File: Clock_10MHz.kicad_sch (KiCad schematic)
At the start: 12 parts, among them U3 74LV8154, U4 74LS151, U8 PCF8574, X1 ASCO

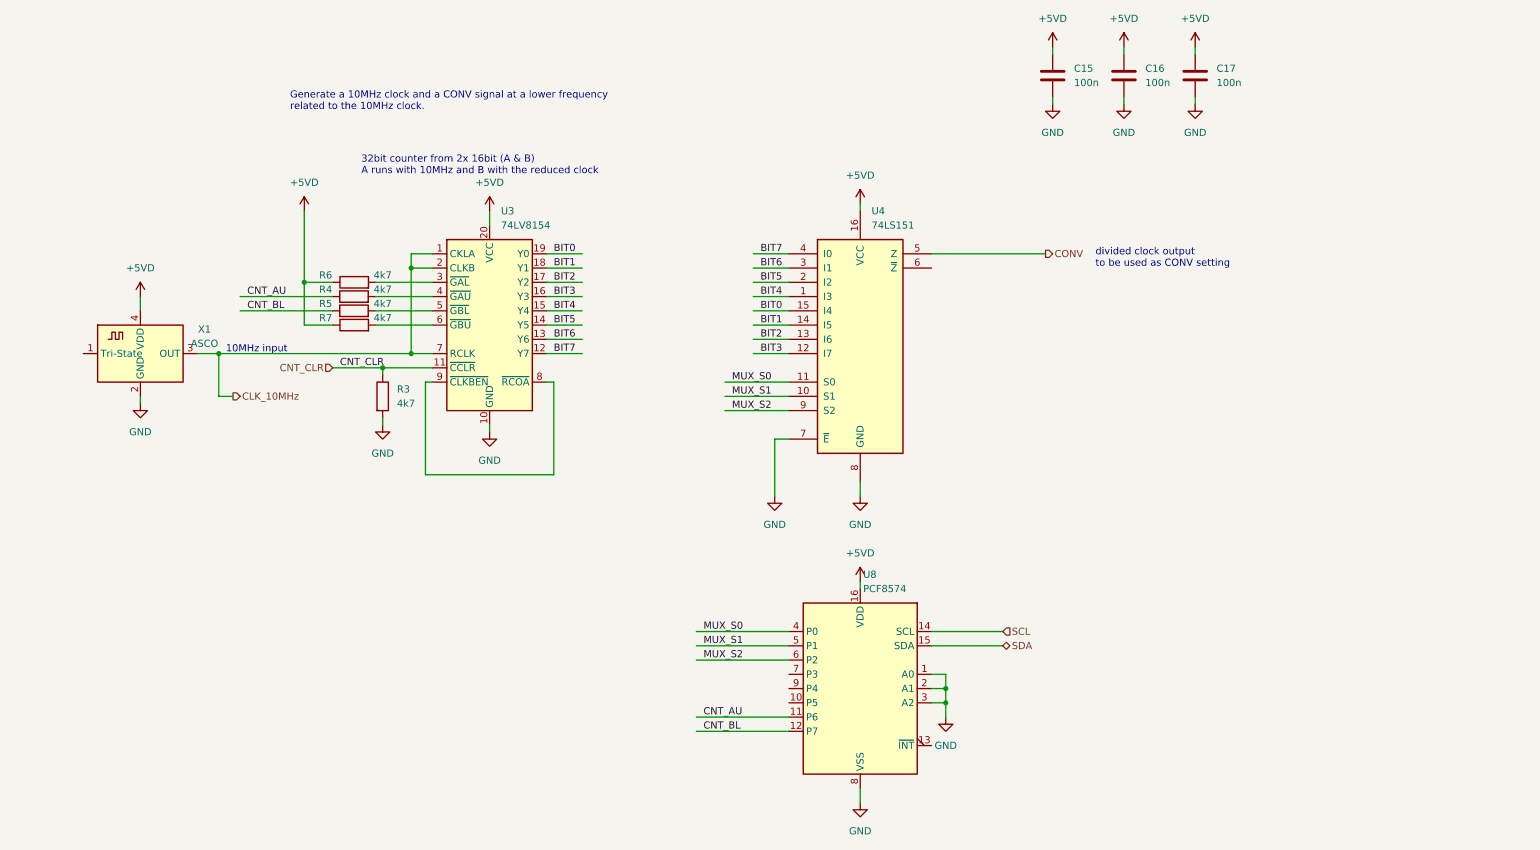
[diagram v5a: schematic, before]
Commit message: updated 10MHz oscillator to DIP 14 package
needs larger PCB space, but much easier to purchase
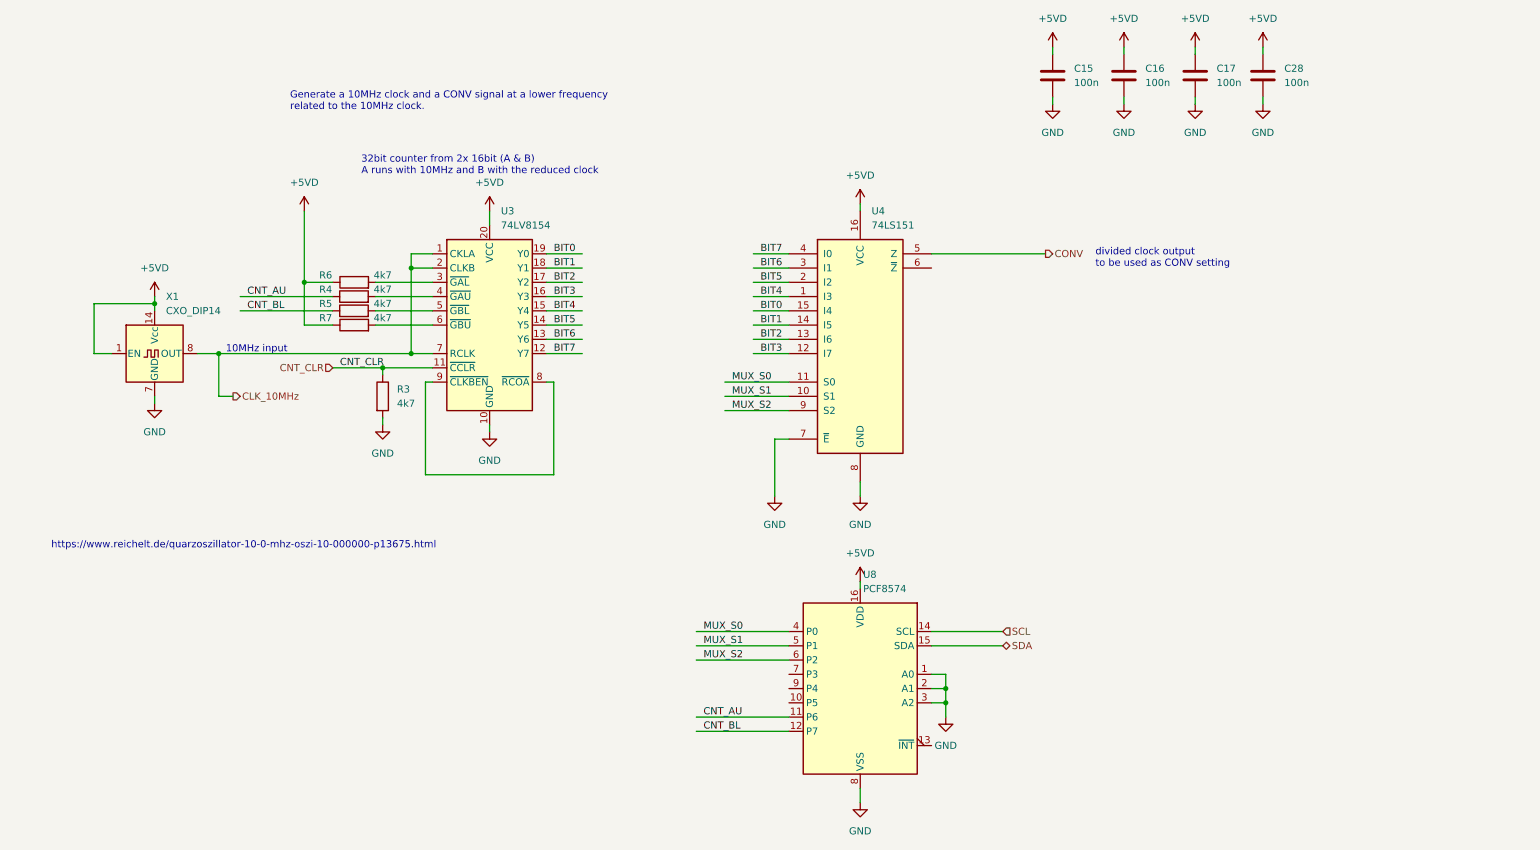
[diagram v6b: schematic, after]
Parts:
- removed X1: ASCO, Oscillator:Oscillator_SMD_Abracon_ASCO-4Pin_1.6x1.2mm, symbol Oscillator:ASCO
- added C28: 100n, Capacitor_SMD:C_0603_1608Metric, symbol Device:C
- added X1: CXO_DIP14, Oscillator:Oscillator_DIP-14, symbol Oscillator:CXO_DIP14
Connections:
- net +5VD: now also C28.1, X1.1 (EN), X1.14 (Vcc)
- net CLK_10MHz: now also X1.8 (OUT)
- net GND: now also C28.2, X1.7 (GND)
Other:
- note added: "https://www.reichelt.de/quarzoszillator-10-0-mhz-oszi-10-000000-p13675.html"
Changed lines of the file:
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@@
   (junction (at 85.09 90.17) (diameter 0) (color 0 0 0 0)
   )
+  (junction (at 39.37 81.28) (diameter 0) (color 0 0 0 0)
+  )
   (junction (at 85.09 74.93) (diameter 0) (color 0 0 0 0)
   )
@@
     (stroke (width 0) (type default) (color 0 0 0 0))
   )
-  (wire (pts (xy 36.83 97.79) (xy 36.83 99.06))
+  (wire (pts (xy 39.37 97.79) (xy 39.37 99.06))
     (stroke (width 0) (type default) (color 0 0 0 0))
   )
@@
     (stroke (width 0) (type default) (color 0 0 0 0))
   )
+  (wire (pts (xy 31.75 90.17) (xy 28.575 90.17))
+    (stroke (width 0) (type default) (color 0 0 0 0))
+  )
   (wire (pts (xy 46.99 90.17) (xy 50.8 90.17))
     (stroke (width 0) (type default) (color 0 0 0 0))
@@
     (stroke (width 0) (type default) (color 0 0 0 0))
   )
+  (wire (pts (xy 28.575 81.28) (xy 39.37 81.28))
+    (stroke (width 0) (type default) (color 0 0 0 0))
+  )
   (wire (pts (xy 85.09 74.93) (xy 88.9 74.93))
     (stroke (width 0) (type default) (color 0 0 0 0))
@@
     (stroke (width 0) (type default) (color 0 0 0 0))
   )
+  (wire (pts (xy 236.855 35.56) (xy 236.855 36.83))
+    (stroke (width 0) (type default) (color 0 0 0 0))
+  )
   (wire (pts (xy 78.7021 80.01) (xy 88.9 80.01))
     (stroke (width 0) (type default) (color 0 0 0 0))
@@
     (stroke (width 0) (type default) (color 0 0 0 0))
   )
+  (wire (pts (xy 236.855 44.45) (xy 236.855 45.72))
+    (stroke (width 0) (type default) (color 0 0 0 0))
+  )
   (wire (pts (xy 177.8 152.4) (xy 180.34 152.4))
     (stroke (width 0) (type default) (color 0 0 0 0))
@@
     (stroke (width 0) (type default) (color 0 0 0 0))
   )
+  (wire (pts (xy 28.575 90.17) (xy 28.575 81.28))
+    (stroke (width 0) (type default) (color 0 0 0 0))
+  )
+  (wire (pts (xy 39.37 81.28) (xy 39.37 82.55))
+    (stroke (width 0) (type default) (color 0 0 0 0))
+  )
   (wire (pts (xy 78.7021 82.55) (xy 88.9 82.55))
     (stroke (width 0) (type default) (color 0 0 0 0))
@@
     (stroke (width 0) (type default) (color 0 0 0 0))
   )
-  (wire (pts (xy 36.83 80.01) (xy 36.83 82.55))
+  (wire (pts (xy 39.37 80.01) (xy 39.37 81.28))
     (stroke (width 0) (type default) (color 0 0 0 0))
   )
@@
   (wire (pts (xy 109.22 72.39) (xy 115.57 72.39))
     (stroke (width 0) (type default) (color 0 0 0 0))
+  )
+  (text "https://www.reichelt.de/quarzoszillator-10-0-mhz-oszi-10-000000-p13675.html"
+    (at 20.955 125.095 0)
+    (effects (font (size 1.27 1.27)) (justify left bottom))
   )
   (text "32bit counter from 2x 16bit (A & B)\nA runs with 10MHz and B with the reduced clock"
@@
     )
     (pin "1")
+  )
+  (symbol (lib_id "Device:C") (at 236.855 40.64 0) (unit 1)
+    (in_bom yes) (on_board yes) (fields_autoplaced)
+    (property "Reference" "C28" (id 0) (at 240.665 39.3699 0)
+      (effects (font (size 1.27 1.27)) (justify left))
+    )
+    (property "Value" "100n" (id 1) (at 240.665 41.9099 0)
+      (effects (font (size 1.27 1.27)) (justify left))
+    )
+    (property "Footprint" "Capacitor_SMD:C_0603_1608Metric" (id 2) (at 237.8202 44.45 0)
+      (effects (font (size 1.27 1.27)) hide)
+    )
+    (property "Datasheet" "~" (id 3) (at 236.855 40.64 0)
+      (effects (font (size 1.27 1.27)) hide)
+    )
+    (pin "1")
+    (pin "2")
   )
   (symbol (lib_id "Device:R") (at 74.93 85.09 90) (unit 1)
@@
     (pin "1")
   )
+  (symbol (lib_id "Oscillator:CXO_DIP14") (at 39.37 90.17 0) (unit 1)
+    (in_bom yes) (on_board yes) (fields_autoplaced)
+    (property "Reference" "X1" (id 0) (at 41.3894 80.01 0)
+      (effects (font (size 1.27 1.27)) (justify left))
+    )
+    (property "Value" "CXO_DIP14" (id 1) (at 41.3894 82.55 0)
+      (effects (font (size 1.27 1.27)) (justify left))
+    )
+    (property "Footprint" "Oscillator:Oscillator_DIP-14" (id 2) (at 50.8 99.06 0)
+      (effects (font (size 1.27 1.27)) hide)
+    )
+    (property "Datasheet" "http://cdn-reichelt.de/documents/datenblatt/B400/OSZI.pdf" (id 3) (at 36.83 90.17 0)
+      (effects (font (size 1.27 1.27)) hide)
+    )
+    (pin "1")
+    (pin "14")
+    (pin "7")
+    (pin "8")
+  )
   (symbol (lib_id "power:GND") (at 99.06 104.14 0) (unit 1)
     (in_bom yes) (on_board yes) (fields_autoplaced)
@@
     )
     (pin "1")
-  )
-  (symbol (lib_id "Oscillator:ASCO") (at 36.83 90.17 0) (unit 1)
-    (in_bom yes) (on_board yes) (fields_autoplaced)
-    (property "Reference" "X1" (id 0) (at 48.26 85.8393 0))
-    (property "Value" "ASCO" (id 1) (at 48.26 88.3793 0))
-    (property "Footprint" "Oscillator:Oscillator_SMD_Abracon_ASCO-4Pin_1.6x1.2mm" (id 2) (at 39.37 99.06 0)
-      (effects (font (size 1.27 1.27)) hide)
-    )
-    (property "Datasheet" "https://abracon.com/Oscillators/ASCO.pdf" (id 3) (at 31.115 86.995 0)
-      (effects (font (size 1.27 1.27)) hide)
-    )
-    (pin "1")
-    (pin "2")
-    (pin "3")
-    (pin "4")
   )
   (symbol (lib_id "power:+5VD") (at 66.04 64.77 0) (unit 1)
@@
     (pin "2")
   )
-  (symbol (lib_id "power:+5VD") (at 36.83 80.01 0) (unit 1)
-    (in_bom yes) (on_board yes) (fields_autoplaced)
-    (property "Reference" "#PWR0112" (id 0) (at 36.83 83.82 0)
-      (effects (font (size 1.27 1.27)) hide)
-    )
-    (property "Value" "+5VD" (id 1) (at 36.83 74.93 0))
-    (property "Footprint" "" (id 2) (at 36.83 80.01 0)
-      (effects (font (size 1.27 1.27)) hide)
-    )
-    (property "Datasheet" "" (id 3) (at 36.83 80.01 0)
-      (effects (font (size 1.27 1.27)) hide)
-    )
-    (pin "1")
-  )
-  (symbol (lib_id "power:GND") (at 36.83 99.06 0) (unit 1)
-    (in_bom yes) (on_board yes) (fields_autoplaced)
-    (property "Reference" "#PWR05" (id 0) (at 36.83 105.41 0)
-      (effects (font (size 1.27 1.27)) hide)
-    )
-    (property "Value" "GND" (id 1) (at 36.83 104.14 0))
-    (property "Footprint" "" (id 2) (at 36.83 99.06 0)
-      (effects (font (size 1.27 1.27)) hide)
-    )
-    (property "Datasheet" "" (id 3) (at 36.83 99.06 0)
+  (symbol (lib_id "power:+5VD") (at 236.855 35.56 0) (unit 1)
+    (in_bom yes) (on_board yes) (fields_autoplaced)
+    (property "Reference" "#PWR053" (id 0) (at 236.855 39.37 0)
+      (effects (font (size 1.27 1.27)) hide)
+    )
+    (property "Value" "+5VD" (id 1) (at 236.855 30.48 0))
+    (property "Footprint" "" (id 2) (at 236.855 35.56 0)
+      (effects (font (size 1.27 1.27)) hide)
+    )
+    (property "Datasheet" "" (id 3) (at 236.855 35.56 0)
+      (effects (font (size 1.27 1.27)) hide)
+    )
+    (pin "1")
+  )
+  (symbol (lib_id "power:+5VD") (at 39.37 80.01 0) (unit 1)
+    (in_bom yes) (on_board yes) (fields_autoplaced)
+    (property "Reference" "#PWR0112" (id 0) (at 39.37 83.82 0)
+      (effects (font (size 1.27 1.27)) hide)
+    )
+    (property "Value" "+5VD" (id 1) (at 39.37 74.93 0))
+    (property "Footprint" "" (id 2) (at 39.37 80.01 0)
+      (effects (font (size 1.27 1.27)) hide)
+    )
+    (property "Datasheet" "" (id 3) (at 39.37 80.01 0)
+      (effects (font (size 1.27 1.27)) hide)
+    )
+    (pin "1")
+  )
+  (symbol (lib_id "power:GND") (at 39.37 99.06 0) (unit 1)
+    (in_bom yes) (on_board yes) (fields_autoplaced)
+    (property "Reference" "#PWR05" (id 0) (at 39.37 105.41 0)
+      (effects (font (size 1.27 1.27)) hide)
+    )
+    (property "Value" "GND" (id 1) (at 39.37 104.14 0))
+    (property "Footprint" "" (id 2) (at 39.37 99.06 0)
+      (effects (font (size 1.27 1.27)) hide)
+    )
+    (property "Datasheet" "" (id 3) (at 39.37 99.06 0)
       (effects (font (size 1.27 1.27)) hide)
     )
@@
       (effects (font (size 1.27 1.27)) hide)
     )
+    (pin "1")
+  )
+  (symbol (lib_id "power:GND") (at 236.855 45.72 0) (unit 1)
+    (in_bom yes) (on_board yes) (fields_autoplaced)
+    (property "Reference" "#PWR054" (id 0) (at 236.855 52.07 0)
+      (effects (font (size 1.27 1.27)) hide)
+    )
+    (property "Value" "GND" (id 1) (at 236.855 50.8 0))
+    (property "Footprint" "" (id 2) (at 236.855 45.72 0)
+      (effects (font (size 1.27 1.27)) hide)
+    )
+    (property "Datasheet" "" (id 3) (at 236.855 45.72 0)
+      (effects (font (size 1.27 1.27)) hide)
+    )

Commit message: inlcuded buffer for 10MHz clock
otherwise the oscillator does not have enough drive strength
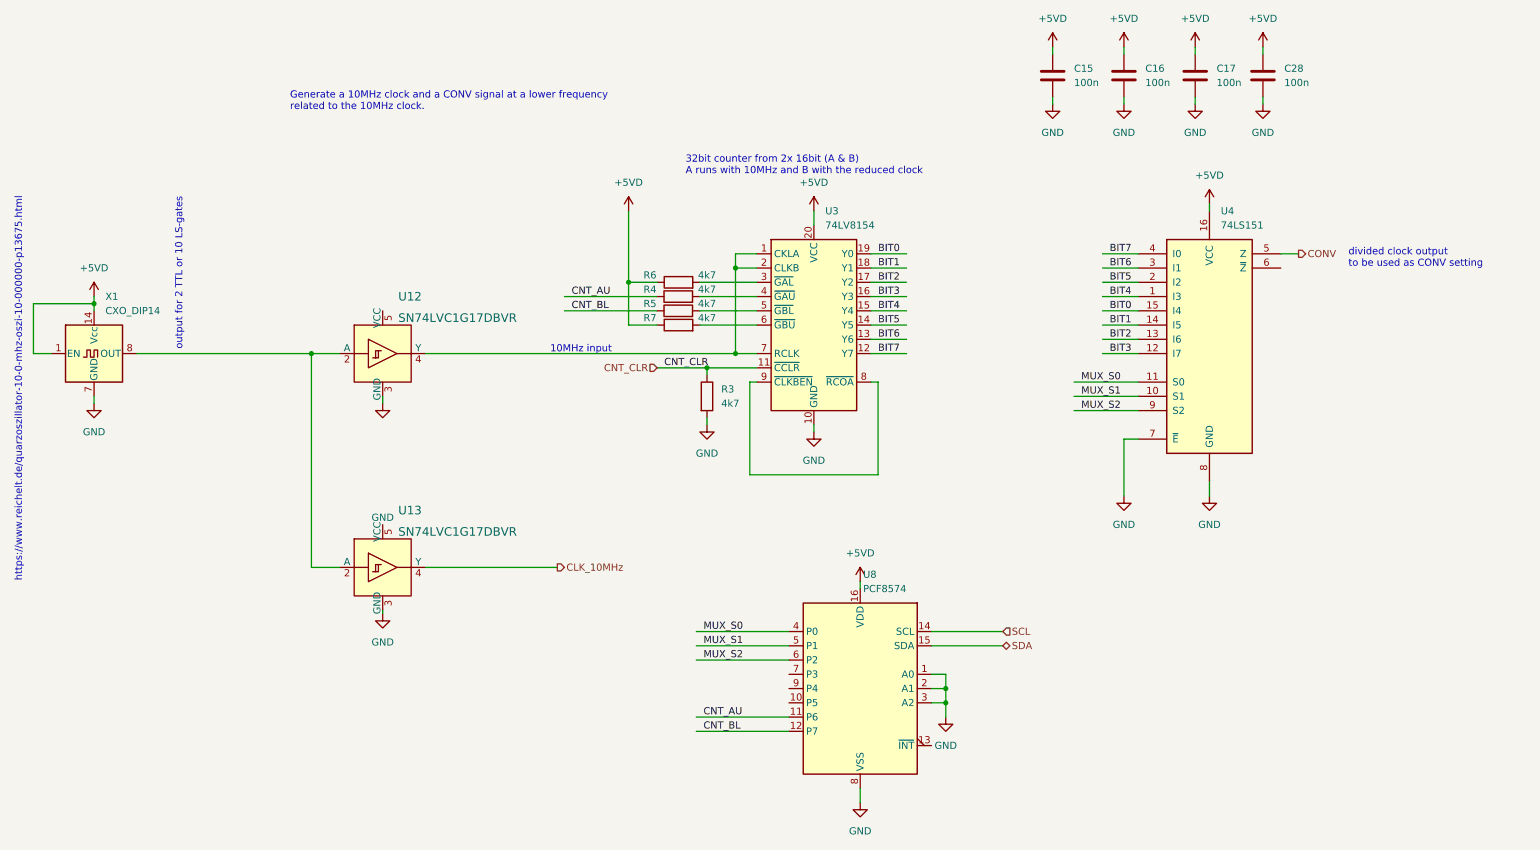
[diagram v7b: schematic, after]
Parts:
- added U12, U13: SN74LVC1G17DBVR, digikey-footprints:SOT-753, symbol dk_Logic-Buffers-Drivers-Receivers-Transceivers:SN74LVC1G17DBVR
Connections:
- net CLK_10MHz: now also U13.4 (Y); no longer U3.1 (CKLA), U3.2 (CLKB), U3.7 (RCLK), X1.8 (OUT)
- net GND: now also U12.3 (GND), U13.3 (GND)
- new net: U12.2 (A), U13.2 (A), X1.8 (OUT)
- new net: U12.4 (Y), U3.1 (CKLA), U3.2 (CLKB), U3.7 (RCLK)
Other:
- note added: "output for 2 TTL or 10 LS-gates"
- moved on the sheet: R3, R4, R5, R6, R7, U3, U4, X1

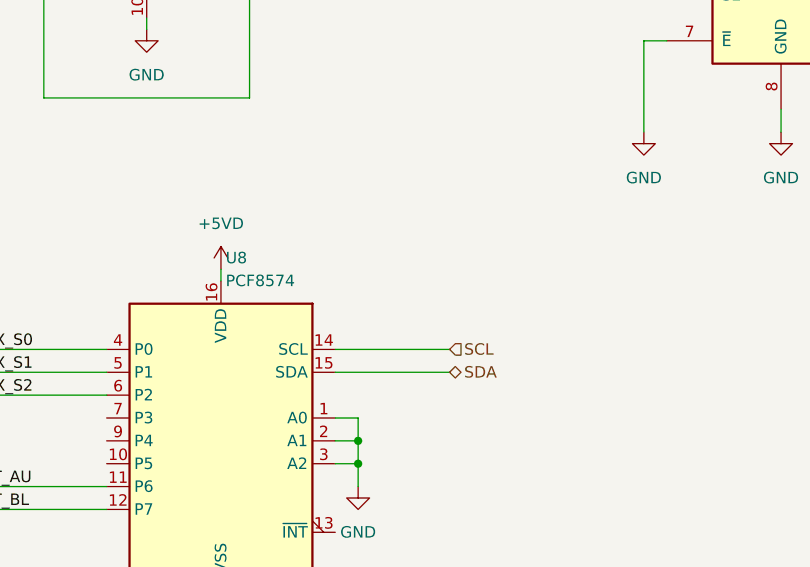
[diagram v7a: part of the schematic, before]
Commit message: added note to PCF8574
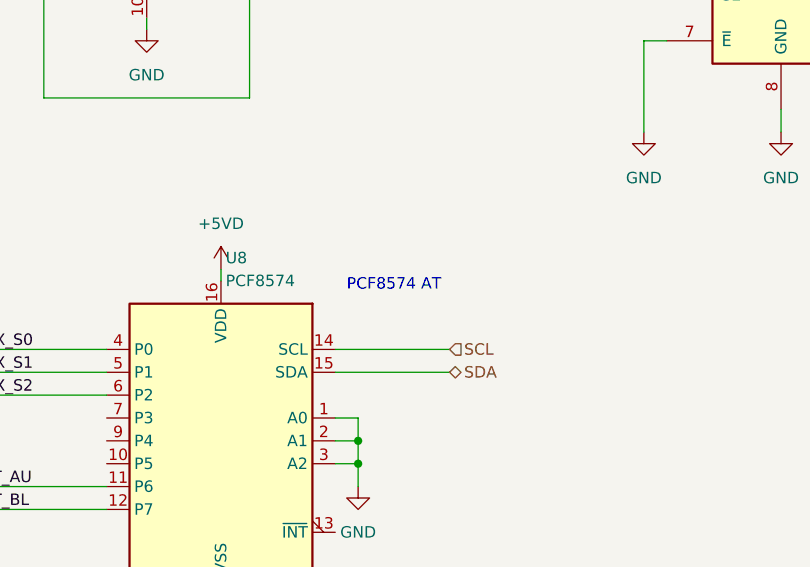
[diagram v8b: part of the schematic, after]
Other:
- note added: "PCF8574 AT"
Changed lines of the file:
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@@
+    (effects (font (size 1.27 1.27)) (justify left bottom))
+  )
+  (text "PCF8574 AT" (at 179.07 133.35 0)
     (effects (font (size 1.27 1.27)) (justify left bottom))
   )
@@
   (symbol (lib_id "power:GND") (at 80.01 136.525 0) (unit 1)
     (in_bom yes) (on_board yes) (fields_autoplaced)
-    (property "Reference" "#PWR?" (id 0) (at 80.01 142.875 0)
+    (property "Reference" "#PWR062" (id 0) (at 80.01 142.875 0)
       (effects (font (size 1.27 1.27)) hide)
     )
@@
   (symbol (lib_id "power:GND") (at 80.01 99.06 0) (unit 1)
     (in_bom yes) (on_board yes)
-    (property "Reference" "#PWR?" (id 0) (at 80.01 105.41 0)
-      (effects (font (size 1.27 1.27)) hide)
-    )
+    (property "Reference" "#PWR061" (id 0) (at 80.01 105.41 0)
+      (effects (font (size 1.27 1.27)) hide)
+    )
